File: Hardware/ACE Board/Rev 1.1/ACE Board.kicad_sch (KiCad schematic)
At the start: 187 parts, among them J1 PHI2 SELECT, J10 PORT A, J11 AUDIO L, J12 DB9 MALE (DTE), J13 PS/2, J14 KEYBOARD, J15 AUDIO R, J16 AUDIO, J17 5V DC, J18 CART, J19 BUS, J2 CTS EN, J20 VCC, J21 POWER LED, J22 STORAGE, J3 RESET SW, J4 DCD EN, J5 VDD, J6 JOYSTICK A, J7 PADDLES, J8 JOYSTICK B, J9 PORT B, SW1 `, SW10 9, SW11 0, SW12 -, SW13 =, SW14 BACKSPACE, SW15 ESCAPE, SW16 TAB, SW17 RESET, SW18 Q, SW19 W, SW2 1, SW20 E, SW21 R, SW22 T, SW23 Y, SW24 U, SW25 I, SW26 O, SW27 P, SW28 [, SW29 ], SW3 2, SW30 \, SW31 INSERT, SW32 CAPS LOCK, SW33 A, SW34 S, SW35 D, SW36 F, SW37 G, SW38 H, SW39 J, SW4 3, SW40 K, SW41 L, SW42 SHIFT, SW43 ;, SW44 ', SW45 ENTER, SW46 DELETE, SW47 Z, SW48 X, SW49 C, SW5 4, SW50 SHIFT, SW51 V, SW52 B, SW53 N, SW54 M, SW55 ,, SW56 ., SW57 /, SW58 UP ARROW, SW59 CTRL, SW6 5, SW60 ALT, SW61 MENU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

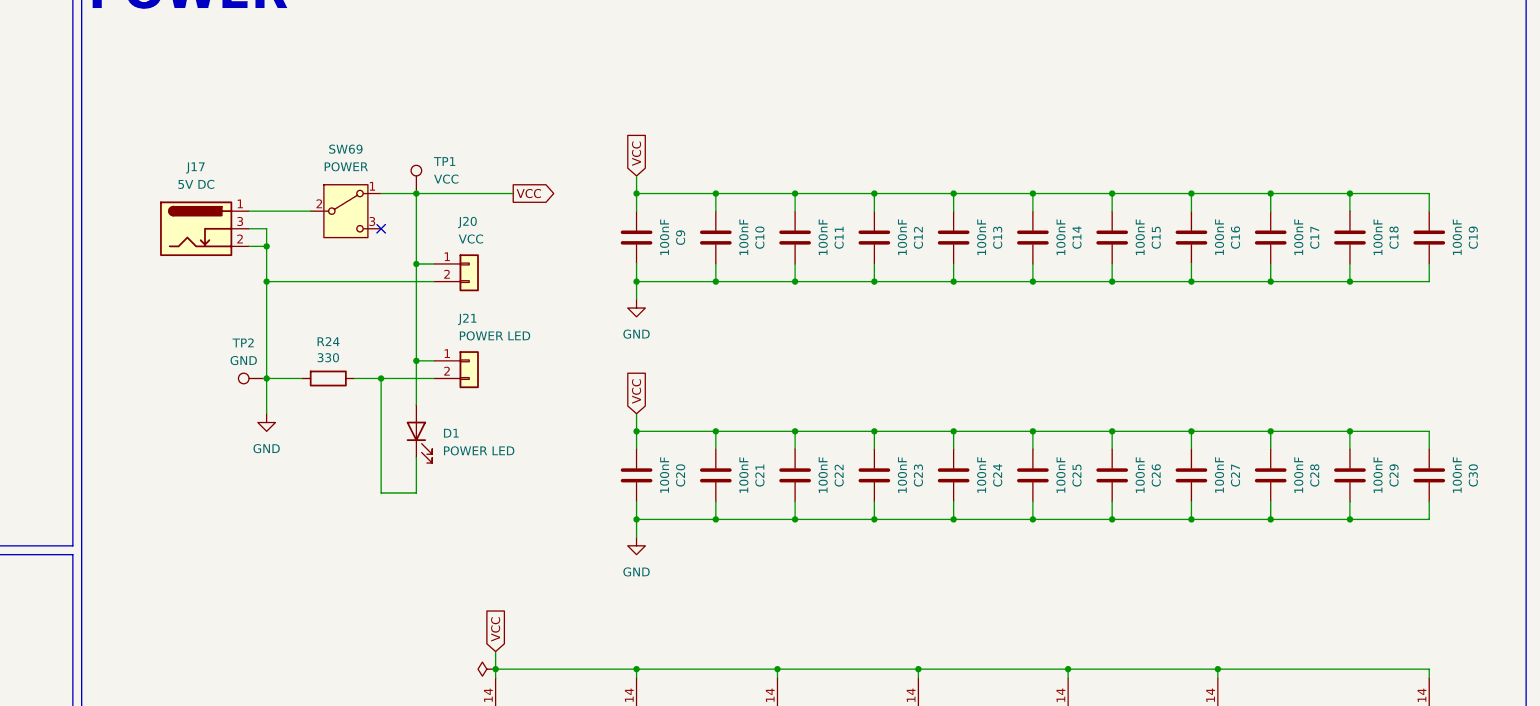
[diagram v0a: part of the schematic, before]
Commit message: Add bulk capacitance to Rev 1.1
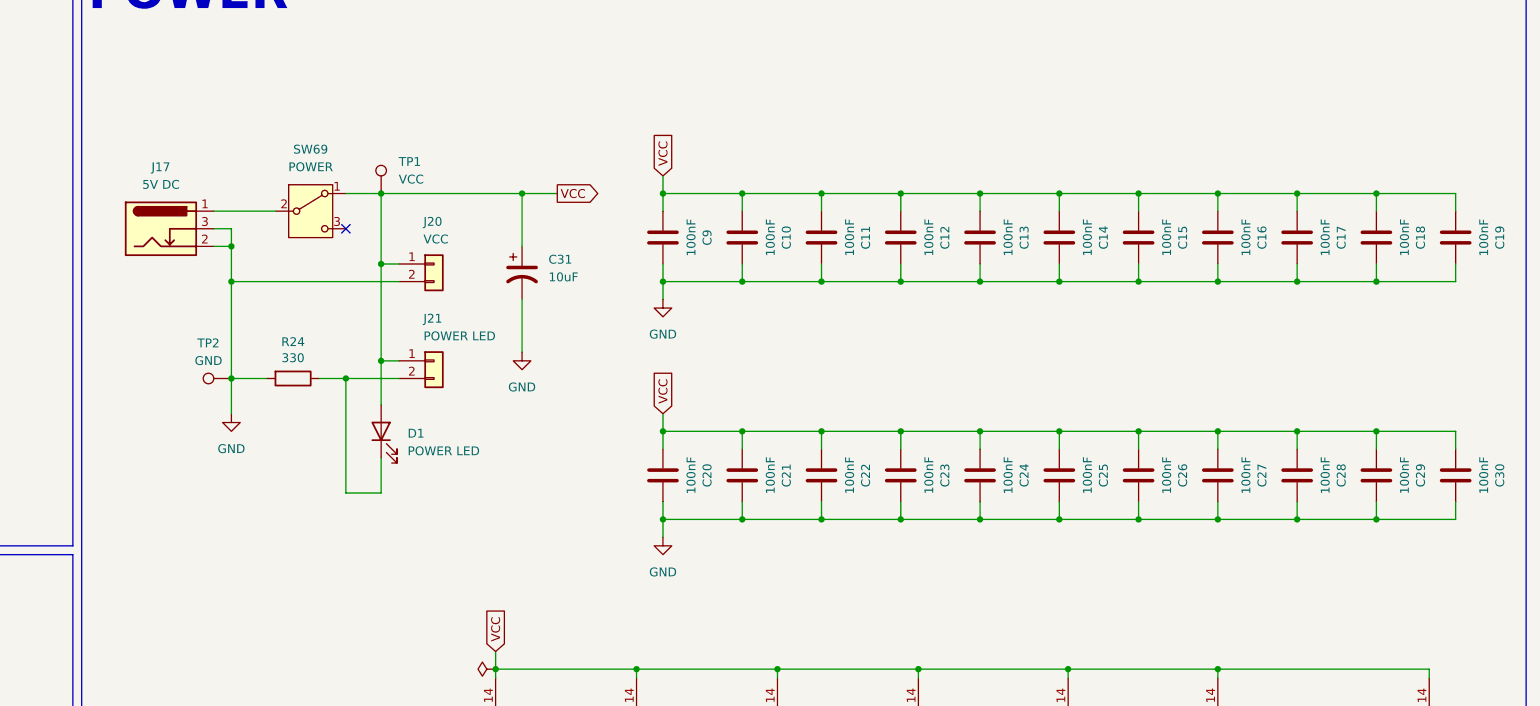
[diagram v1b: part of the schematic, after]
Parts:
- added C31: 10uF, Capacitor_THT:CP_Radial_D4.0mm_P1.50mm, symbol Device:C_Polarized_US
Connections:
- net GND: now also C31.2
- net VCC: now also C31.1
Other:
- moved on the sheet: C10, C11, C12, C13, C14, C15, C16, C17, C18, C19, C20, C21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
